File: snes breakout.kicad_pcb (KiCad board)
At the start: 2 copper layers, 10 parts, among them J1 Conn_01x12_Male, J2 Mini-DIN-4, J3 Conn_01x09_Female, J4 DB15_Female_HighDensity_Mount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, J5 AudioJack3

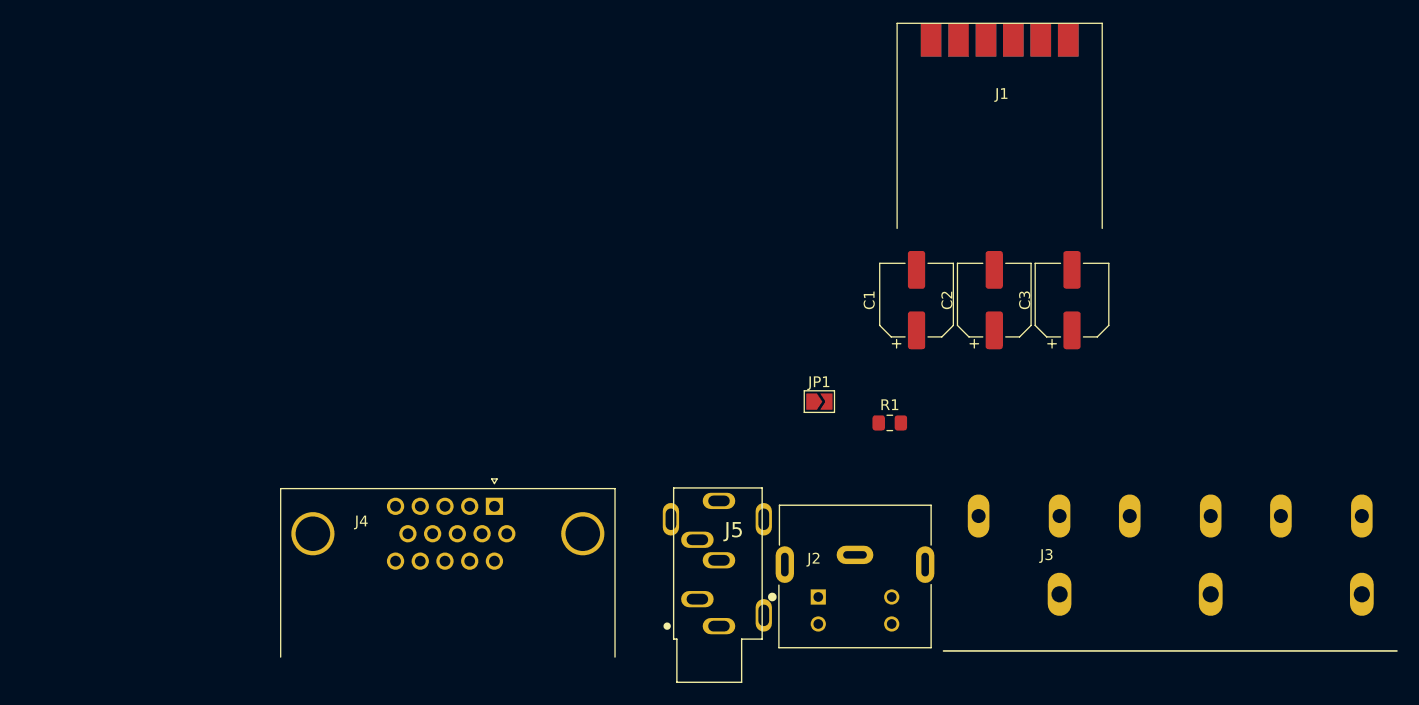
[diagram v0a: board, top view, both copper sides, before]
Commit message: laid outline, placed components
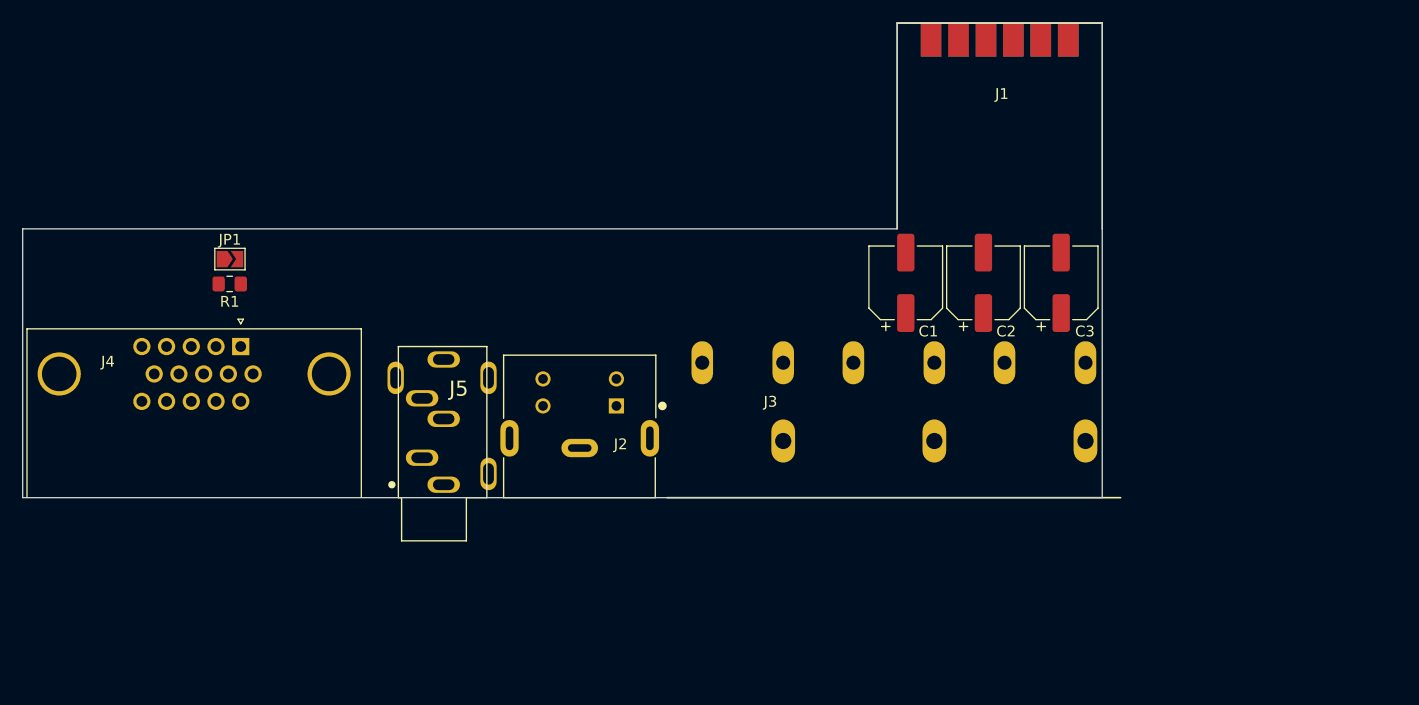
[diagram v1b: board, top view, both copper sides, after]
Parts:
- moved R1 62.5 mm to (102.8, 49.9), turned to 180 degrees
- moved JP1 56.2 mm to (102.8, 47.6)
- moved J3 29.3 mm to (164.3, 69.7)
- moved J2 29.0 mm to (135.2, 63.1), turned to 180 degrees
- moved J5 28.7 mm to (122.6, 68.5)
- moved J4 27.8 mm to (103.8, 55.7)
- moved C1 1.89 mm to (165.4, 49.8)
- moved C2 1.89 mm to (172.6, 49.8)
- moved C3 1.89 mm to (179.8, 49.8)
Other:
- board outline added: 100 x 44 mm

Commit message: Laid tracks, generated gerbers
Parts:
- added REF**: MountingHole_5.3mm_M5, MountingHole:MountingHole_5.3mm_M5, F.Cu at (133.6, 49.8)
- added REF**: MountingHole_3.2mm_M3, MountingHole:MountingHole_3.2mm_M3, F.Cu at (155.8, 49.8)
- added REF**: MountingHole_3.2mm_M3, MountingHole:MountingHole_3.2mm_M3, F.Cu at (88.6, 49.8)
- turned C1 to 270 degrees
- turned C2 to 270 degrees
- turned C3 to 270 degrees
- turned JP1 to 180 degrees
- turned R1 to 0 degrees
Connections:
- J2 pad S1: (no net) -> GND
- J2 pad S2: (no net) -> GND
- J2 pad S3: (no net) -> GND
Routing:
- net RED_OUT: track 0.00 -> 107.2 mm
- net RIGHT: track 0.00 -> 99.7 mm
- net LEFT: track 0.00 -> 96.9 mm, vias 0 -> 1
- net CSYNC: track 0.00 -> 92.9 mm
- net BLUE_OUT: track 0.00 -> 88.9 mm, vias 0 -> 1
- net CHROMA: track 0.00 -> 79.0 mm
- net GREEN_OUT: track 0.00 -> 78.5 mm
- net LUMA: track 0.00 -> 57.5 mm
- net CVBS: track 0.00 -> 54.0 mm
- net VGA_SYNC_OUT: track 0.00 -> 25.4 mm
- net BLUE: track 0.00 -> 23.6 mm, vias 0 -> 1
- net GREEN: track 0.00 -> 21.7 mm, vias 0 -> 1
- net RED: track 0.00 -> 20.7 mm
- net GND: vias 0 -> 45
- added copper zone on B.Cu, net GND
- added copper zone on F.Cu, net GND
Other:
- board text added: "Close for TTL CSYNC"
- board text added: "SNES BREAKOUT 1.0 Tinkerplunk"

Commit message: Generated gerbers
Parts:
- removed the REF** at (133.6, 49.8)
- added REF**: MountingHole_5.5mm, MountingHole:MountingHole_5.5mm, F.Cu at (133.6, 49.8)
- R1: footprint Resistor_SMD:R_0805_2012Metric_Pad1.15x1.40mm_HandSolder -> Resistor_SMD:R_0603_1608Metric_Pad1.05x0.95mm_HandSolder
- moved REF** 1.40 mm to (90.0, 49.8)
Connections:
- J2 pad S1: GND -> (no net)
- J2 pad S2: GND -> (no net)
- J2 pad S3: GND -> (no net)
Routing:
- net GND: vias 45 -> 44
- net (no net): vias 0 -> 1
